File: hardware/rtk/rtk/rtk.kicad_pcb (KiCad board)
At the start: 4 copper layers, 76.2 x 66 mm, 90 parts, among them J1 USB4105-GF-A, J10 Conn_01x02_Pin, J11 Conn_01x06_Pin, J3 B2B-PH-SM4-TBLFSN, J4 Conn_01x02_Pin, J5 Conn_Coaxial, J6 MEM2052-00-195-00-A_REVA, J7 Conn_01x04_Pin, J8 Conn_01x01_Pin, J9 Conn_01x08_Pin, U1 BQ24075RGT, U2 TPS63020DSJR, U3 STM32F765VITx, U4 ZED-F9H-01B, U5 ESP32-S3-ZERO, U6 CORE1262-868M, U7 LSM6DSOX, U8 USB3300-EZK, U9 USBLC6-2SC6, Y1 ASTX-H11-16.000MHZ-T, Y2 ASTX-H11-24.000MHZ-T

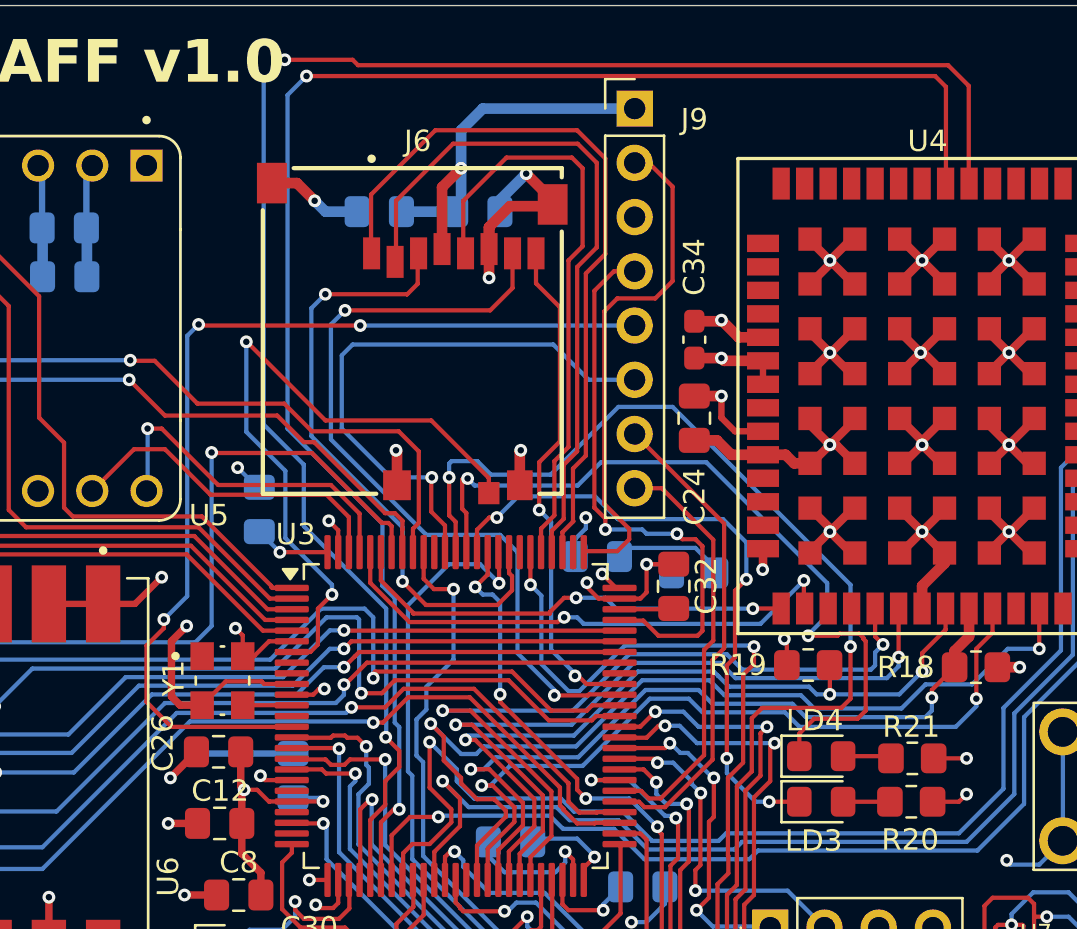
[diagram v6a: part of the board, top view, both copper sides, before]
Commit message: Connect F9P UART2 (corrections port) to STM32 UART7
PA8 (UART7_RX) → F9P TXD2, PA15 (UART7_TX) → F9P RXD2.
Dedicated channel for RTCM correction data, keeping UART1 free
for navigation output and UBX configuration.

Co-Authored-By: Claude Sonnet 4.6 <noreply@anthropic.com>
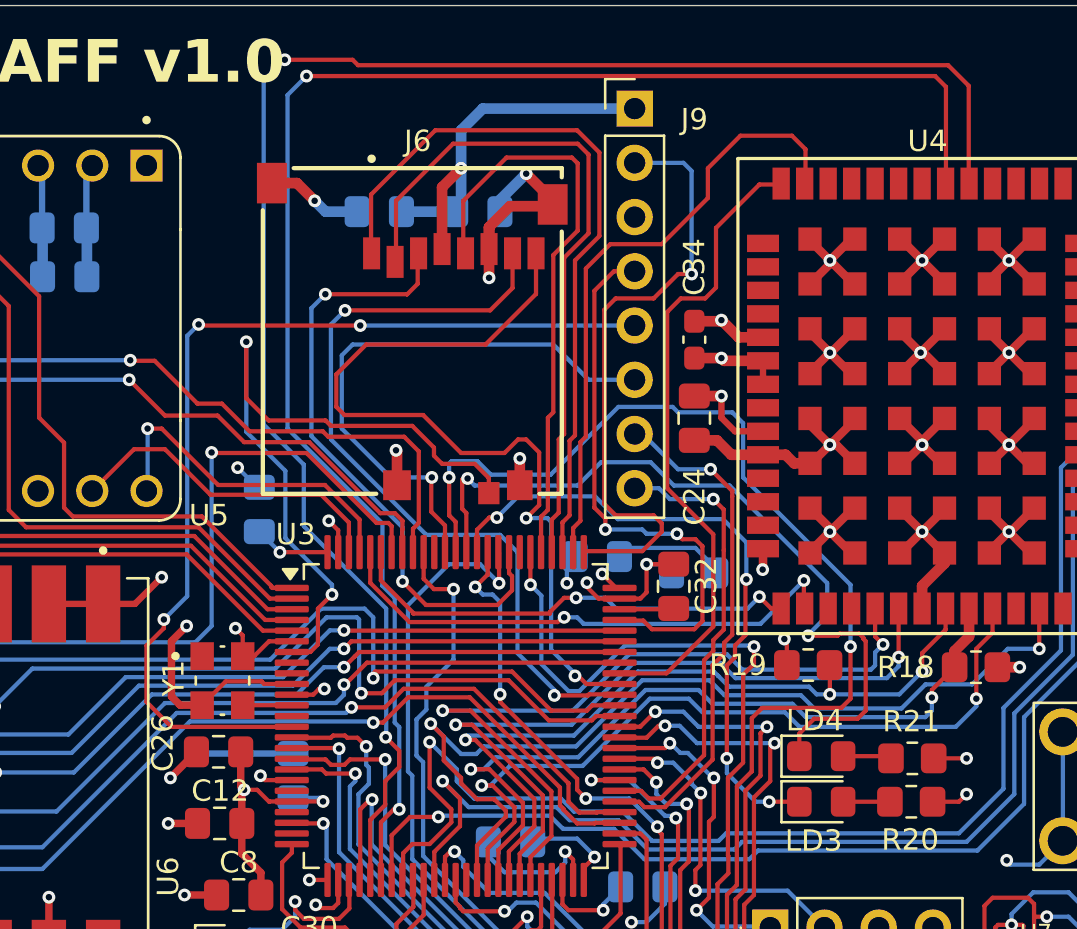
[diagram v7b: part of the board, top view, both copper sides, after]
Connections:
- net F9P_RX renamed UART5_RX_F9P_TXD
- net F9P_TX renamed UART5_TX_F9P_RXD
- U2 pad V: (no net) -> GND
- U3 pad 67: unconnected-(U3-PA8-Pad67) -> UART7_RX_F9P_TXD2
- U3 pad 77: unconnected-(U3-PA15-Pad77) -> UART7_TX_F9P_RXD2
- U4 pad 26: unconnected-(U4A-RXD2-Pad26) -> UART7_TX_F9P_RXD2
- U4 pad 27: unconnected-(U4A-TXD2-Pad27) -> UART7_RX_F9P_TXD2
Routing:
- net UART7_RX_F9P_TXD2: track 0.00 -> 30.4 mm
- net UART7_TX_F9P_RXD2: track 0.00 -> 29.1 mm
- net SDMMC_D1: track 23.8 -> 40.0 mm
- net PA14/SWCLK: track 24.0 -> 29.7 mm, vias 0 -> 1
- net SDMMC_CD: track 32.2 -> 34.0 mm
- net PD9/DEBUG_RX: track 19.9 -> 21.4 mm, vias 0 -> 1
- net SYSOFF: track 83.1 -> 84.6 mm
- net PD8/DEBUG_TX: track 22.6 -> 24.0 mm, vias 0 -> 1
- net GND: track 283.8 -> 282.7 mm
- net PA13/SWDIO: track 26.8 -> 26.3 mm

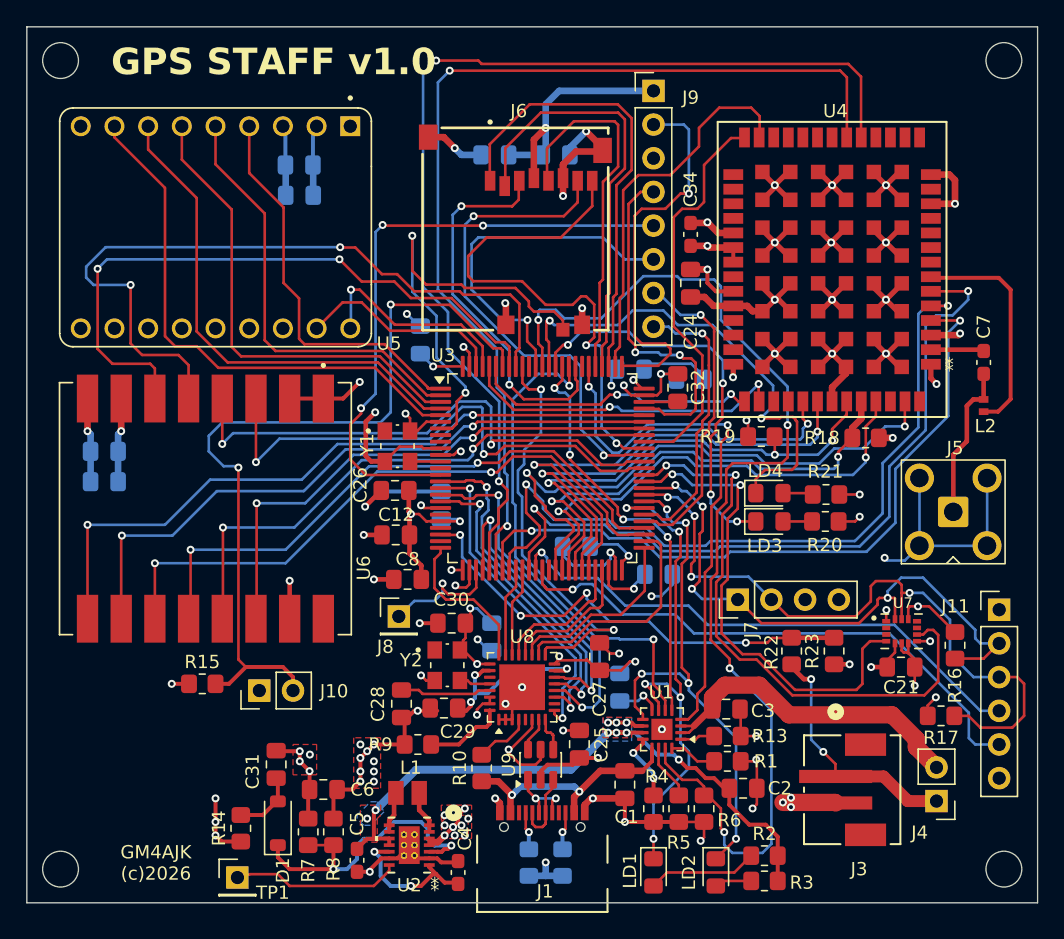
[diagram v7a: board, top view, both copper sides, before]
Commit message: Schematic/PCB/ioc: mode-select jumper, ESD swap, routing updates
PA0 (BASE_ROVER_MODE_SELECT) added to ioc with pull-up, FB1 removed
from schematic, USBLC6-4SC6 replaces out-of-stock USBLC6-2SC6,
PCB routing updates from design review session.

Co-Authored-By: Claude Sonnet 4.6 <noreply@anthropic.com>
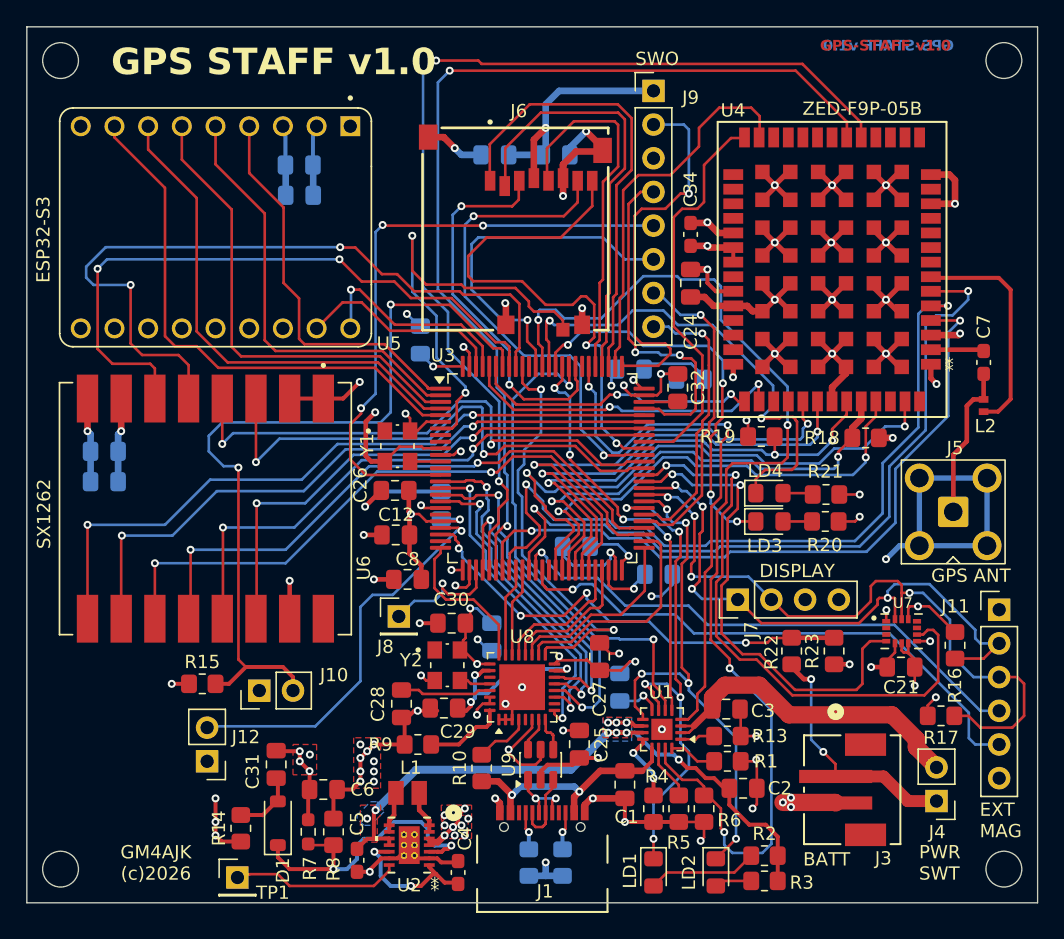
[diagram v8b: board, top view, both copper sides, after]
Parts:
- added J12: Conn_01x02_Pin, Connector_PinHeader_2.54mm:PinHeader_1x02_P2.54mm_Vertical, F.Cu at (115.2, 141.7)
- R7: footprint Resistor_SMD:R_0805_2012Metric_Pad1.20x1.40mm_HandSolder -> Resistor_SMD:R_0603_1608Metric_Pad0.98x0.95mm_HandSolder
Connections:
- U2 pad V: GND -> (no net)
- U3 pad 22: unconnected-(U3-PA0-Pad22) -> Net-(J12-Pin_2)
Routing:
- net Net-(J12-Pin_2): track 0.00 -> 30.3 mm, vias 0 -> 1
- net GND: track 282.7 -> 287.6 mm
- net F9P_GEOFENCE_STAT: track 79.2 -> 77.1 mm
- net F9P_RTK_STAT: track 75.4 -> 73.4 mm
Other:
- board text added: "BATT"
- board text added: "DISPLAY"
- board text added: "ESP32-S3"
- board text added: "EXT MAG"
- board text added: "GPS ANT"
- board text added: "GPS-STAFF v1.0"
- board text added: "PWR SWT"
- board text added: "SWO"
- board text added: "SX1262"
- board text added: "ZED-F9P-05B"
